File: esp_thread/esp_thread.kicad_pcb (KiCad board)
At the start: 2 copper layers, 68.2 x 61.2 mm, 1 part, among them U1 113991254

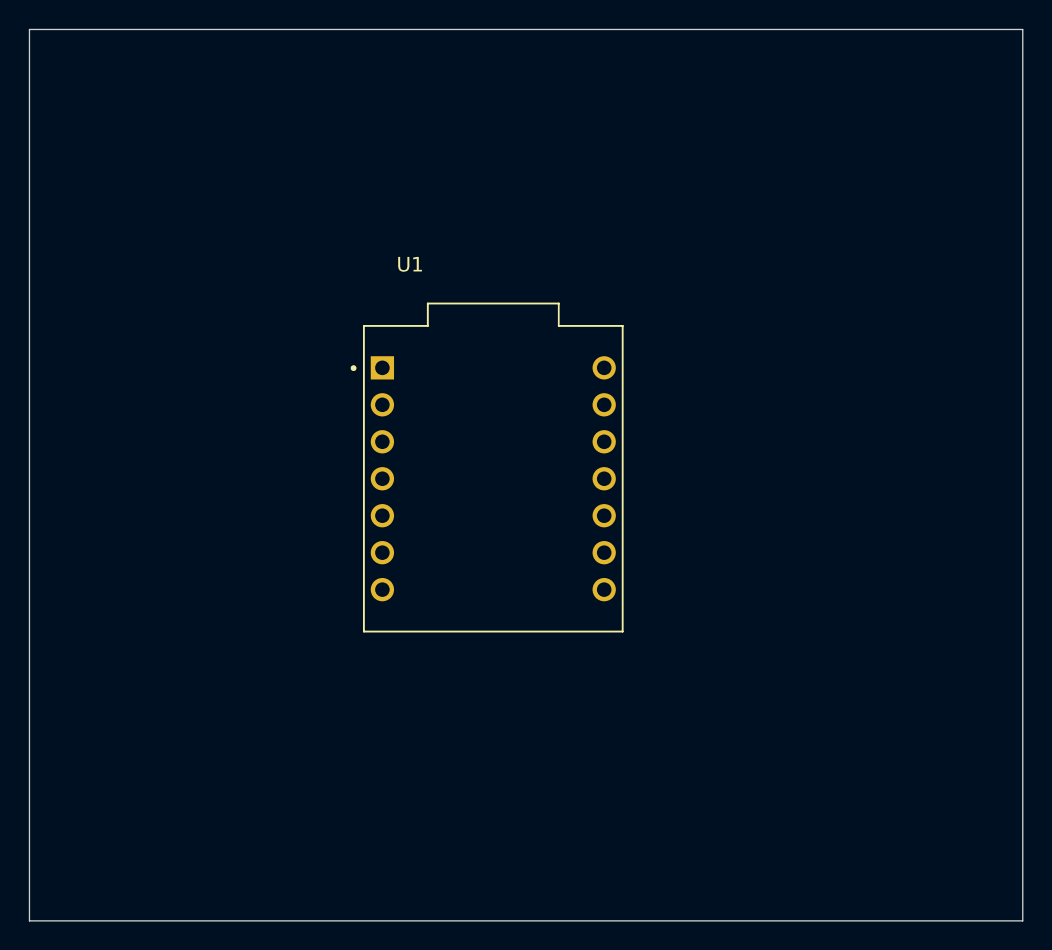
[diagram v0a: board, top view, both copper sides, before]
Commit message: Add temperature sensor comparison script and output files, light PCB almost done, button PCB and temperature PCB in progress
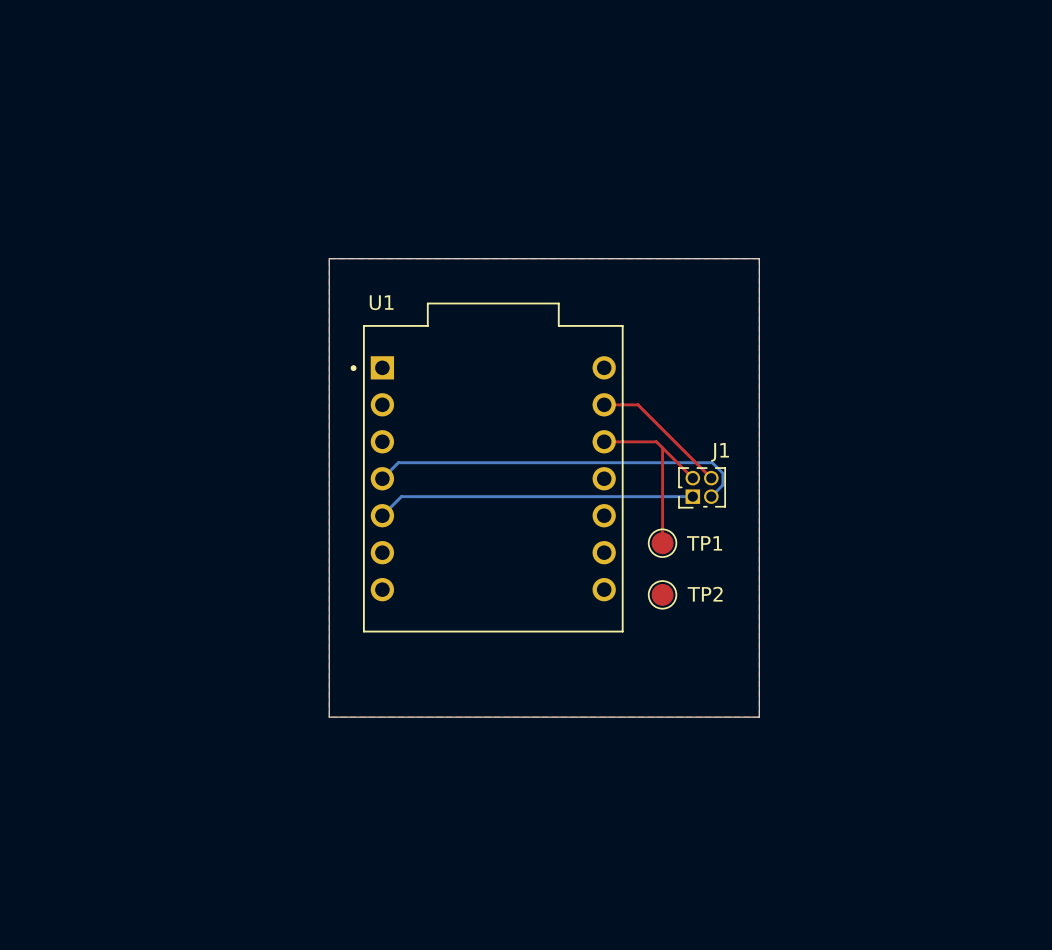
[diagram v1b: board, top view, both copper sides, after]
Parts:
- added J1: Conn_02x02_Counter_Clockwise, Connector_PinSocket_1.27mm:PinSocket_2x02_P1.27mm_Vertical, F.Cu at (158.6, 98.6)
- added TP1: TestPoint, TestPoint:TestPoint_Pad_D1.5mm, F.Cu at (156.5, 101.8)
- added TP2: TestPoint, TestPoint:TestPoint_Pad_D1.5mm, F.Cu at (156.5, 105.3)
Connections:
- U1 pad 4: unconnected-(U1-D3-Pad4) -> /SDA
- U1 pad 5: unconnected-(U1-D4-Pad5) -> /SCL
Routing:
- net /SDA: track 0.00 -> 26.1 mm
- net /SCL: track 0.00 -> 21.9 mm
- net +3V3: track 0.00 -> 13.7 mm
- net GND: track 0.00 -> 9.45 mm
- added copper zone on F.Cu, net GND
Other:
- board size 68.2 x 61.2 mm -> 29.6 x 31.5 mm
